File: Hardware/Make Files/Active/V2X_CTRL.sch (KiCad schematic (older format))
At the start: 38 parts, among them CON1 AVR-PDI-6, IC1 ATXMEGA16A4U-A, P20 Jumper 1, P21 Jumper 2, P22 CONN_02X04, P23 Jumper 3, P24 Jumper 4, Q16 2N7000, Q17 2N7000, Q18 2N7000, Q19 2N7000, U21 74LS126, U22 74HC595, U23 74HC595

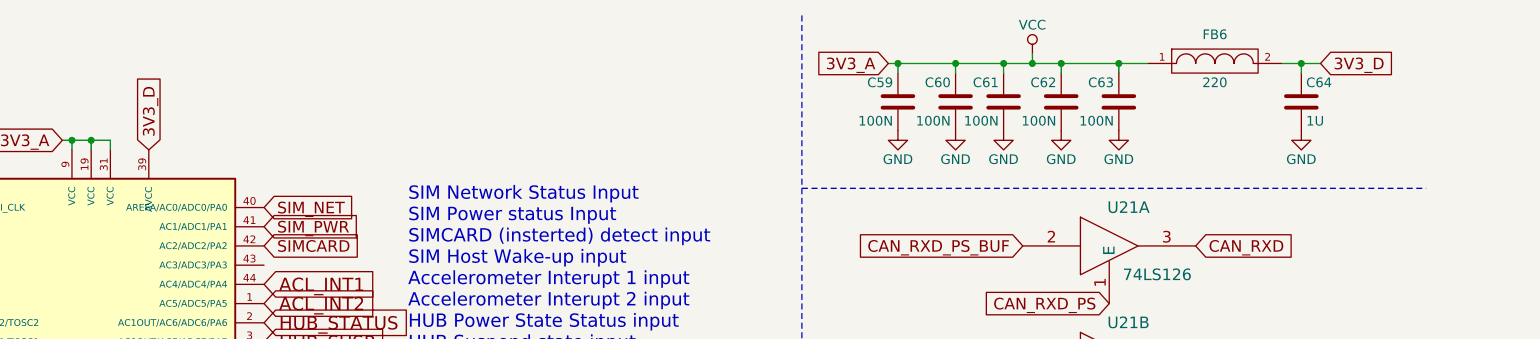
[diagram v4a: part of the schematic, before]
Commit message: Build pass of main V2X board
ready to verify
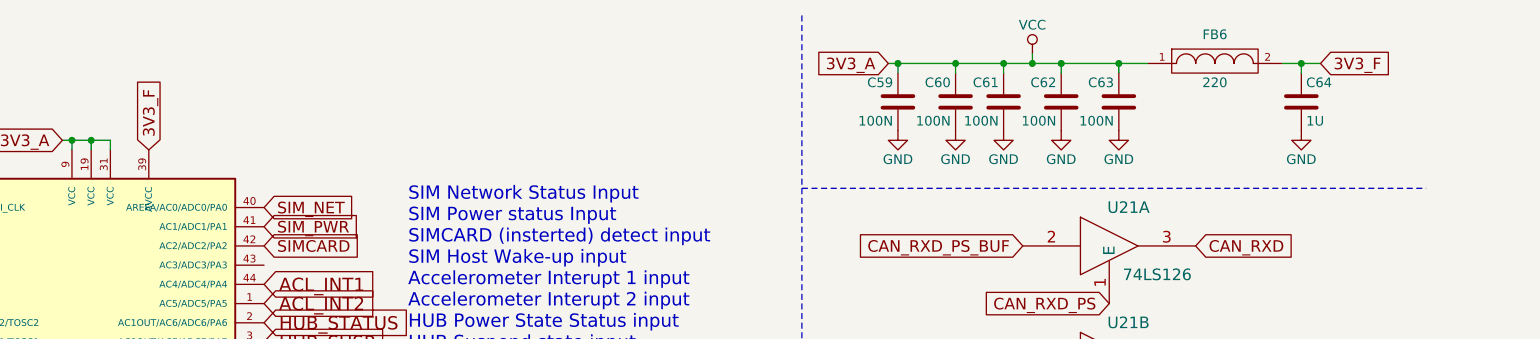
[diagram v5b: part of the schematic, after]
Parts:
- Q16, Q17, Q18, Q19: footprint Housings_SOT-23_SOT-143_TSOT-6:SOT-23 -> Custom Parts:SOT-23-123
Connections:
- net labels added: 3V3_F
- net labels removed: 3V3_D
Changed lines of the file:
@@
 SEQ_LED2
 $Comp
-L GND #PWR0140
+L GND #PWR0139
 U 1 1 55F86E9C
 P 4100 3900
-F 0 "#PWR0140" H 4100 3650 50  0001 C CNN
+F 0 "#PWR0139" H 4100 3650 50  0001 C CNN
 F 1 "GND" H 4100 3750 50  0000 C CNN
 F 2 "" H 4100 3900 60  0000 C CNN
@@
 	8900 5850 8900 5950
 $Comp
-L GND #PWR0141
+L GND #PWR0140
 U 1 1 55F86EC1
 P 8900 6250
-F 0 "#PWR0141" H 8900 6000 50  0001 C CNN
+F 0 "#PWR0140" H 8900 6000 50  0001 C CNN
 F 1 "GND" H 8900 6100 50  0000 C CNN
 F 2 "" H 8900 6250 60  0000 C CNN
@@
 	4100 1150 4350 1150
 Text GLabel 4550 1200 1    60   Input ~ 0
-3V3_D
+3V3_F
 Text GLabel 3350 1600 0    60   Input ~ 0
 PDI
@@
 PDI
 $Comp
-L GND #PWR0142
+L GND #PWR0141
 U 1 1 55F86EF0
 P 10050 4850
-F 0 "#PWR0142" H 10050 4600 50  0001 C CNN
+F 0 "#PWR0141" H 10050 4600 50  0001 C CNN
 F 1 "GND" H 10050 4700 50  0000 C CNN
 F 2 "" H 10050 4850 60  0000 C CNN
@@
 5V0_B_EN
 $Comp
-L GND #PWR0143
+L GND #PWR0142
 U 1 1 55FA434A
 P 1100 5750
-F 0 "#PWR0143" H 1100 5500 50  0001 C CNN
+F 0 "#PWR0142" H 1100 5500 50  0001 C CNN
 F 1 "GND" H 1100 5600 50  0000 C CNN
 F 2 "" H 1100 5750 60  0000 C CNN
@@
 $EndComp
 $Comp
-L GND #PWR0144
+L GND #PWR0143
 U 1 1 55FA46C8
 P 1100 7150
-F 0 "#PWR0144" H 1100 6900 50  0001 C CNN
+F 0 "#PWR0143" H 1100 6900 50  0001 C CNN
 F 1 "GND" H 1100 7000 50  0000 C CNN
 F 2 "" H 1100 7150 60  0000 C CNN
@@
 $EndComp
 $Comp
-L GND #PWR0145
+L GND #PWR0144
 U 1 1 55FD726F
 P 5850 7350
-F 0 "#PWR0145" H 5850 7100 50  0001 C CNN
+F 0 "#PWR0144" H 5850 7100 50  0001 C CNN
 F 1 "GND" H 5850 7200 50  0000 C CNN
 F 2 "" H 5850 7350 60  0000 C CNN
@@
 $EndComp
 $Comp
-L GND #PWR0146
+L GND #PWR0145
 U 1 1 55FD7284
 P 5500 7500
-F 0 "#PWR0146" H 5500 7250 50  0001 C CNN
+F 0 "#PWR0145" H 5500 7250 50  0001 C CNN
 F 1 "GND" H 5500 7350 50  0000 C CNN
 F 2 "" H 5500 7500 60  0000 C CNN
@@
 $EndComp
 $Comp
-L GND #PWR0147
+L GND #PWR0146
 U 1 1 55FD7672
 P 6350 7500
-F 0 "#PWR0147" H 6350 7250 50  0001 C CNN
+F 0 "#PWR0146" H 6350 7250 50  0001 C CNN
 F 1 "GND" H 6350 7350 50  0000 C CNN
 F 2 "" H 6350 7500 60  0000 C CNN
@@
 PC_LED2
 $Comp
-L GND #PWR0148
+L GND #PWR0147
 U 1 1 55FD7660
 P 6700 7350
-F 0 "#PWR0148" H 6700 7100 50  0001 C CNN
+F 0 "#PWR0147" H 6700 7100 50  0001 C CNN
 F 1 "GND" H 6700 7200 50  0000 C CNN
 F 2 "" H 6700 7350 60  0000 C CNN
@@
 F 0 "Q16" H 6200 4500 50  0000 R CNN
 F 1 "2N7000" H 6300 4250 50  0000 R CNN
-F 2 "Housings_SOT-23_SOT-143_TSOT-6:SOT-23" H 6500 4500 29  0001 C CNN
+F 2 "Custom Parts:SOT-23-123" H 6500 4500 29  0001 C CNN
 F 3 "http://www.mouser.com/ds/2/149/2N7002K-102052.pdf" H 6300 4400 60  0001 C CNN
 F 4 "512-2N7002K" H 6300 4400 60  0001 C CNN "Mouse PN"
@@
 $EndComp
 $Comp
-L GND #PWR0149
+L GND #PWR0148
 U 1 1 55FE1020
 P 6400 4600
-F 0 "#PWR0149" H 6400 4350 50  0001 C CNN
+F 0 "#PWR0148" H 6400 4350 50  0001 C CNN
 F 1 "GND" H 6400 4450 50  0000 C CNN
 F 2 "" H 6400 4600 60  0000 C CNN
@@
 HUB_SUSP
 Text GLabel 10650 750  2    60   Input ~ 0
-3V3_D
+3V3_F
 Wire Wire Line
 	10450 750  10650 750
@@
 Connection ~ 10550 750
 $Comp
-L GND #PWR0150
+L GND #PWR0149
 U 1 1 56006FBB
 P 10550 1100
-F 0 "#PWR0150" H 10550 850 50  0001 C CNN
+F 0 "#PWR0149" H 10550 850 50  0001 C CNN
 F 1 "GND" H 10550 950 50  0000 C CNN
 F 2 "" H 10550 1100 60  0000 C CNN
@@
 Connection ~ 9000 750
 $Comp
-L GND #PWR0151
+L GND #PWR0150
 U 1 1 560285A0
 P 9000 1100
-F 0 "#PWR0151" H 9000 850 50  0001 C CNN
+F 0 "#PWR0150" H 9000 850 50  0001 C CNN
 F 1 "GND" H 9000 950 50  0000 C CNN
 F 2 "" H 9000 1100 60  0000 C CNN
@@
 $EndComp
 $Comp
-L GND #PWR0152
+L GND #PWR0151
 U 1 1 560285F6
 P 9300 1100
-F 0 "#PWR0152" H 9300 850 50  0001 C CNN
+F 0 "#PWR0151" H 9300 850 50  0001 C CNN
 F 1 "GND" H 9300 950 50  0000 C CNN
 F 2 "" H 9300 1100 60  0000 C CNN
@@
 $EndComp
 $Comp
-L GND #PWR0153
+L GND #PWR0152
 U 1 1 5602864C
 P 9600 1100
-F 0 "#PWR0153" H 9600 850 50  0001 C CNN
+F 0 "#PWR0152" H 9600 850 50  0001 C CNN
 F 1 "GND" H 9600 950 50  0000 C CNN
 F 2 "" H 9600 1100 60  0000 C CNN
@@
 Connection ~ 9150 750
 $Comp
-L VCC #PWR0154
+L VCC #PWR0153
 U 1 1 56029609
 P 9150 700
-F 0 "#PWR0154" H 9150 550 50  0001 C CNN
+F 0 "#PWR0153" H 9150 550 50  0001 C CNN
 F 1 "VCC" H 9150 850 50  0000 C CNN
 F 2 "" H 9150 700 60  0000 C CNN
@@
 Connection ~ 8750 750
 $Comp
-L GND #PWR0155
+L GND #PWR0154
 U 1 1 5602C4DB
 P 8750 1100
-F 0 "#PWR0155" H 8750 850 50  0001 C CNN
+F 0 "#PWR0154" H 8750 850 50  0001 C CNN
 F 1 "GND" H 8750 950 50  0000 C CNN
 F 2 "" H 8750 1100 60  0000 C CNN
@@
 $EndComp
 $Comp
-L GND #PWR0156
+L GND #PWR0155
 U 1 1 5602C537
 P 8450 1100
-F 0 "#PWR0156" H 8450 850 50  0001 C CNN
+F 0 "#PWR0155" H 8450 850 50  0001 C CNN
 F 1 "GND" H 8450 950 50  0000 C CNN
 F 2 "" H 8450 1100 60  0000 C CNN
@@
 F 0 "Q18" H 6900 7200 50  0000 R CNN
 F 1 "2N7000" H 7100 7100 50  0000 R CNN
-F 2 "Housings_SOT-23_SOT-143_TSOT-6:SOT-23" H 6800 7250 29  0001 C CNN
+F 2 "Custom Parts:SOT-23-123" H 6800 7250 29  0001 C CNN
 F 3 "http://www.mouser.com/ds/2/149/2N7002K-102052.pdf" H 6600 7150 60  0001 C CNN
 F 4 "512-2N7002K" H 6600 7150 60  0001 C CNN "Mouse PN"
@@
 F 0 "Q17" H 6050 7200 50  0000 R CNN
 F 1 "2N7000" H 6250 7100 50  0000 R CNN
-F 2 "Housings_SOT-23_SOT-143_TSOT-6:SOT-23" H 5950 7250 29  0001 C CNN
+F 2 "Custom Parts:SOT-23-123" H 5950 7250 29  0001 C CNN
 F 3 "http://www.mouser.com/ds/2/149/2N7002K-102052.pdf" H 5750 7150 60  0001 C CNN
 F 4 "512-2N7002K" H 5750 7150 60  0001 C CNN "Mouse PN"
@@
 $EndComp
 $Comp
-L GND #PWR0157
+L GND #PWR0156
 U 1 1 560D95B8
 P 5000 7350
-F 0 "#PWR0157" H 5000 7100 50  0001 C CNN
+F 0 "#PWR0156" H 5000 7100 50  0001 C CNN
 F 1 "GND" H 5000 7200 50  0000 C CNN
 F 2 "" H 5000 7350 60  0000 C CNN
@@
 $EndComp
 $Comp
-L GND #PWR0158
+L GND #PWR0157
 U 1 1 560D95C5
 P 4650 7500
-F 0 "#PWR0158" H 4650 7250 50  0001 C CNN
+F 0 "#PWR0157" H 4650 7250 50  0001 C CNN
 F 1 "GND" H 4650 7350 50  0000 C CNN
 F 2 "" H 4650 7500 60  0000 C CNN
@@
 F 0 "Q19" H 5200 7200 50  0000 R CNN
 F 1 "2N7000" H 5400 7100 50  0000 R CNN
-F 2 "Housings_SOT-23_SOT-143_TSOT-6:SOT-23" H 5100 7250 29  0001 C CNN
+F 2 "Custom Parts:SOT-23-123" H 5100 7250 29  0001 C CNN
 F 3 "http://www.mouser.com/ds/2/149/2N7002K-102052.pdf" H 4900 7150 60  0001 C CNN
 F 4 "512-2N7002K" H 4900 7150 60  0001 C CNN "Mouse PN"
@@
 $EndComp
 $Comp
-L GND #PWR0159
+L GND #PWR0158
 U 1 1 560DBE9F
 P 1650 1300
-F 0 "#PWR0159" H 1650 1050 50  0001 C CNN
+F 0 "#PWR0158" H 1650 1050 50  0001 C CNN
 F 1 "GND" H 1650 1150 50  0000 C CNN
 F 2 "" H 1650 1300 60  0000 C CNN

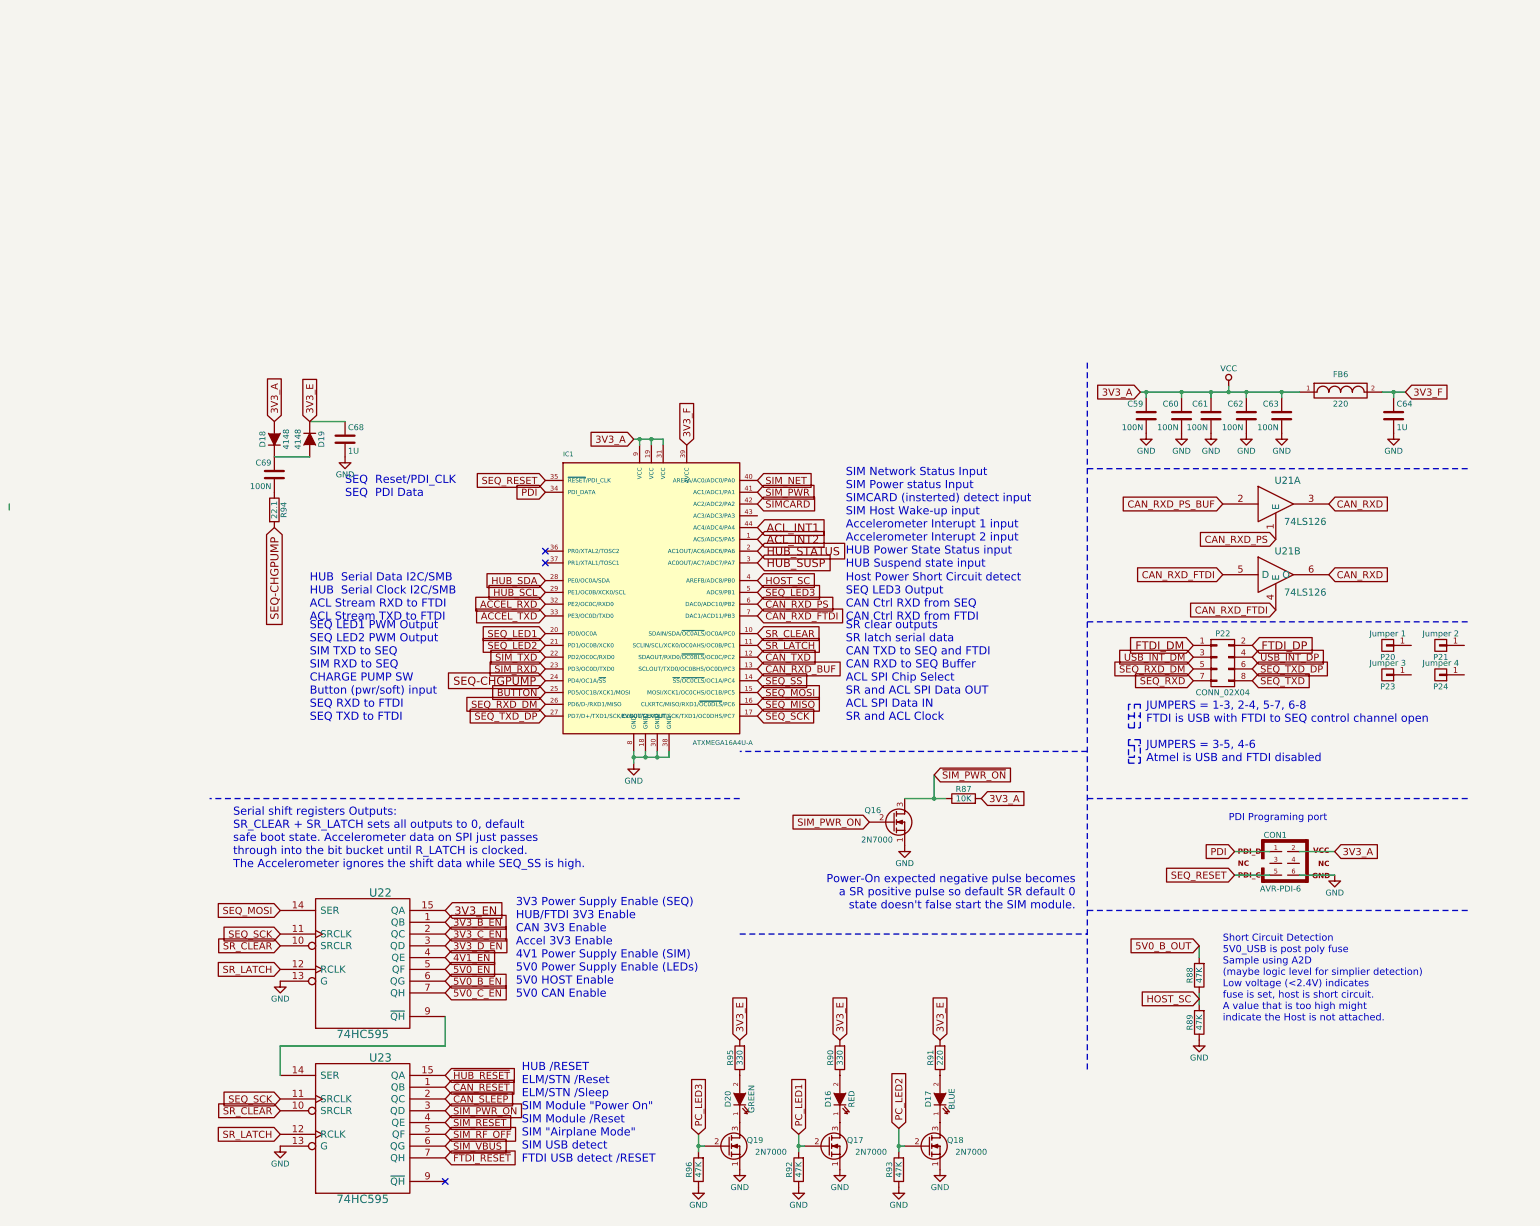
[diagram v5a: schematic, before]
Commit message: Project rework
Split the Main and GSM boards into separate projects, redesigned Main
board after flaws were found.
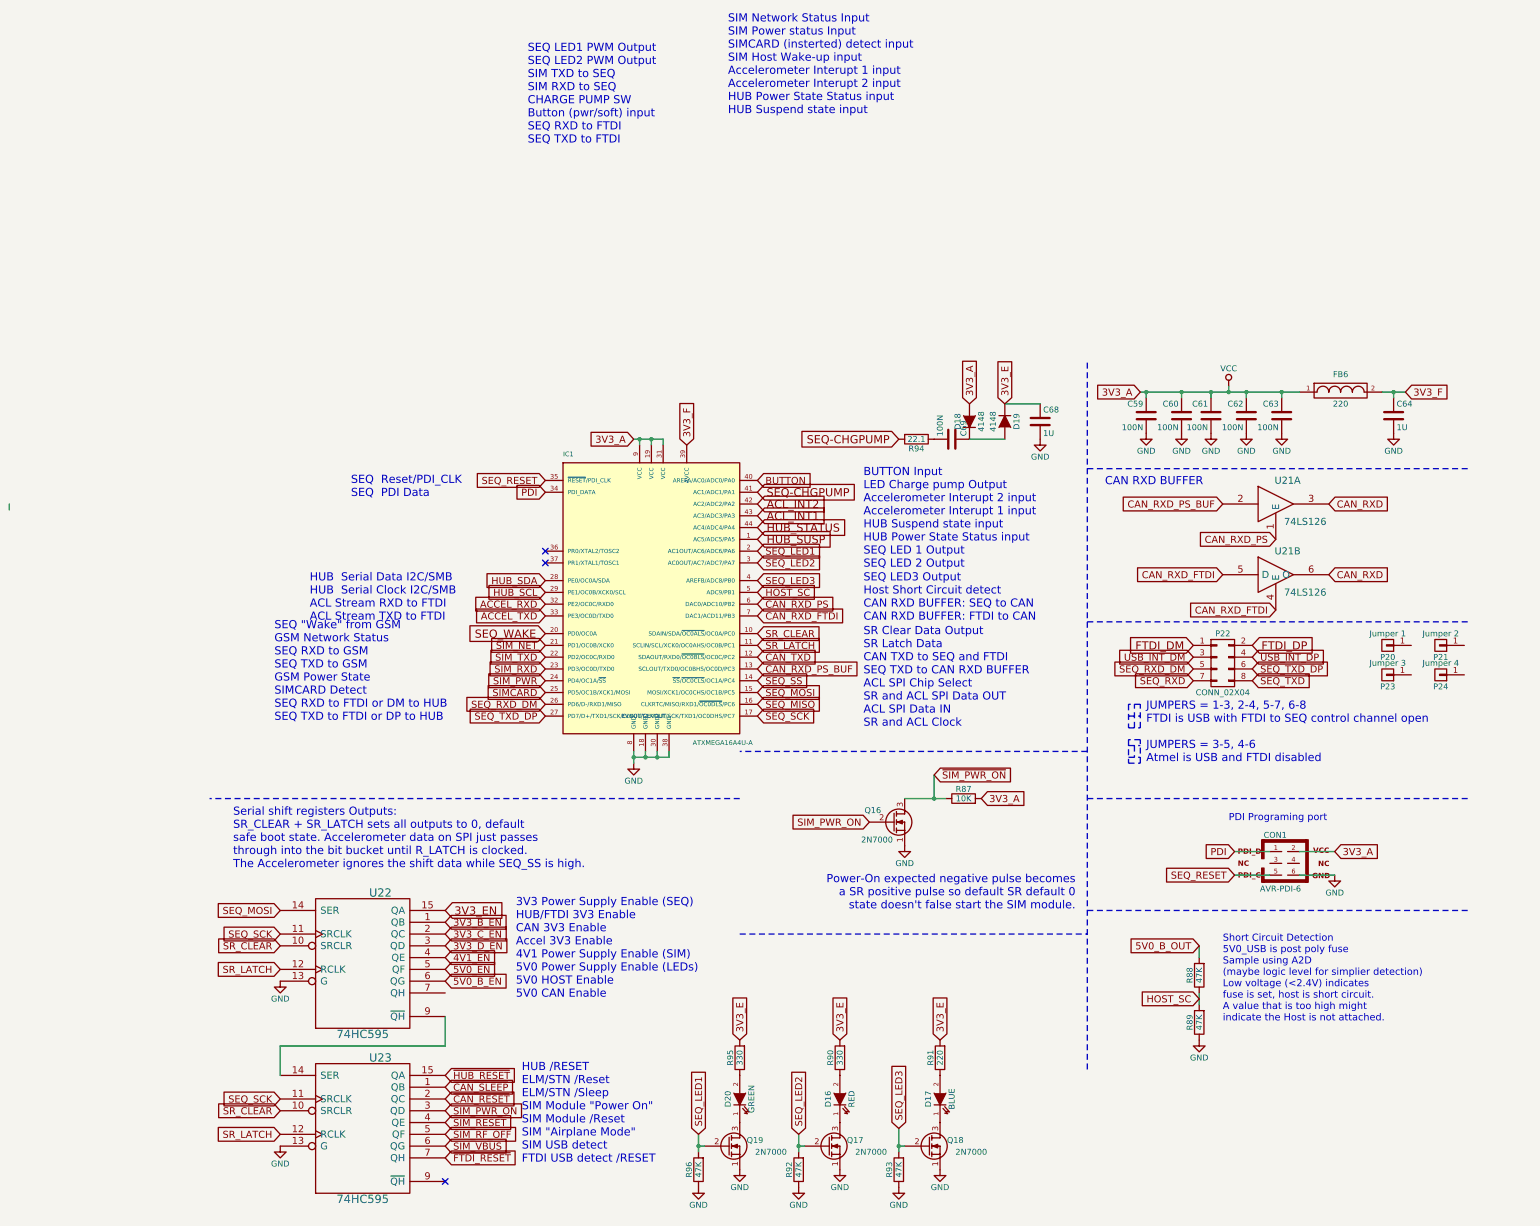
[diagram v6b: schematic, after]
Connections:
- net labels added: SEQ_WAKE
- net labels removed: 5V0_C_EN, CAN_RXD_BUF, PC_LED1, PC_LED2, PC_LED3
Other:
- note added: "BUTTON Input\nLED Charge pump Output\nAccelerometer Interupt 2 input\nAccelerometer Interupt 1 input\nHUB Suspend state input\nHUB Power State Status input\nSEQ LED 1 Output\nSEQ LED 2 Output"
- note added: "CAN RXD BUFFER"
- note added: "SEQ "Wake" from GSM\nGSM Network Status\nSEQ RXD to GSM\nSEQ TXD to GSM\nGSM Power State\nSIMCARD Detect\nSEQ RXD to FTDI or DM to HUB\nSEQ TXD to FTDI or DP to HUB"
- note added: "SEQ LED3 Output\nHost Short Circuit detect\nCAN RXD BUFFER: SEQ to CAN \nCAN RXD BUFFER: FTDI to CAN"
- note added: "SR Clear Data Output\nSR Latch Data \nCAN TXD to SEQ and FTDI\nSEQ TXD to CAN RXD BUFFER\nACL SPI Chip Select\nSR and ACL SPI Data OUT\nACL SPI Data IN\nSR and ACL Clock"
- note removed: "Host Power Short Circuit detect\nSEQ LED3 Output\nCAN Ctrl RXD from SEQ\nCAN Ctrl RXD from FTDI"
- note removed: "SR clear outputs\nSR latch serial data \nCAN TXD to SEQ and FTDI\nCAN RXD to SEQ Buffer\nACL SPI Chip Select\nSR and ACL SPI Data OUT\nACL SPI Data IN\nSR and ACL Clock"
- moved on the sheet: C68, C69, D18, D19, R94
